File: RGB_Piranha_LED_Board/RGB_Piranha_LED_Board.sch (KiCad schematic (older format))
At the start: 20 parts, among them J1 Conn_01x04, J2 Conn_01x04

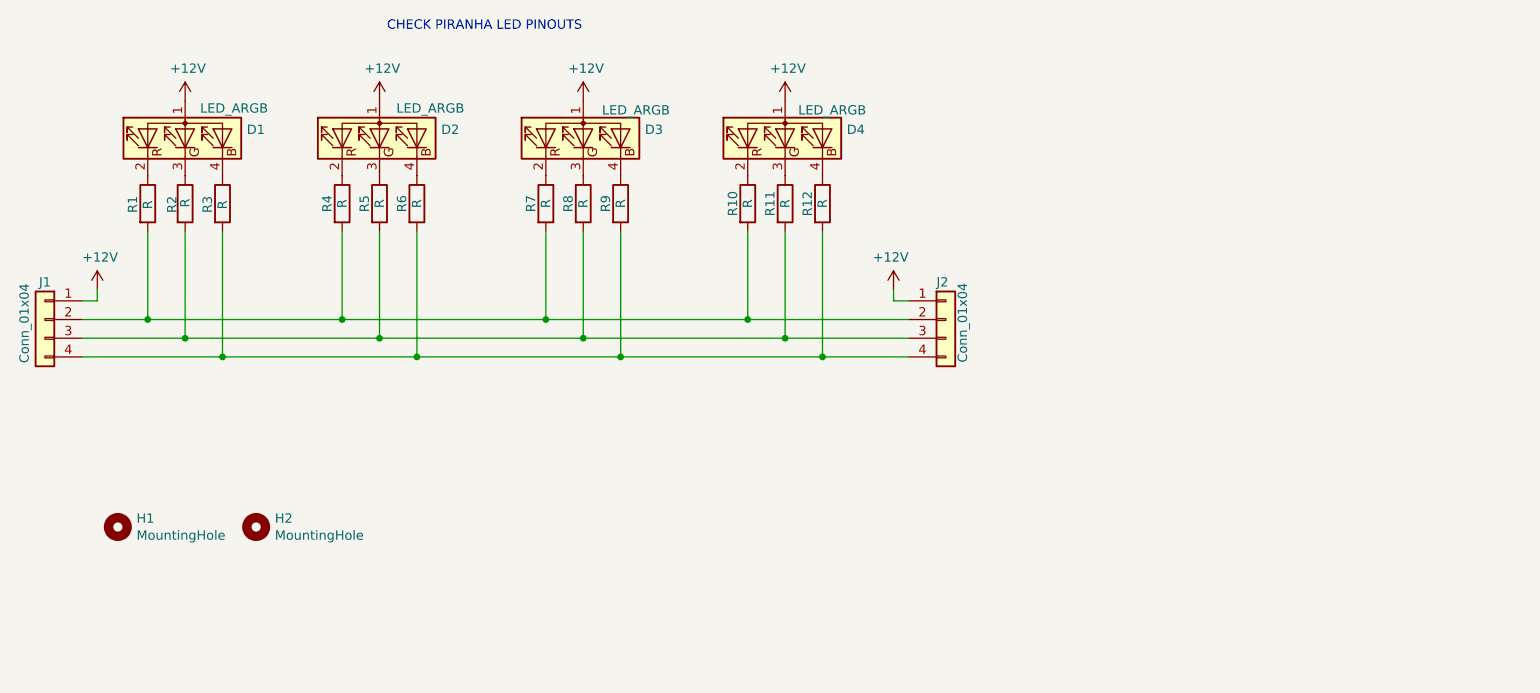
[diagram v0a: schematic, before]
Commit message: added custom LED footprint
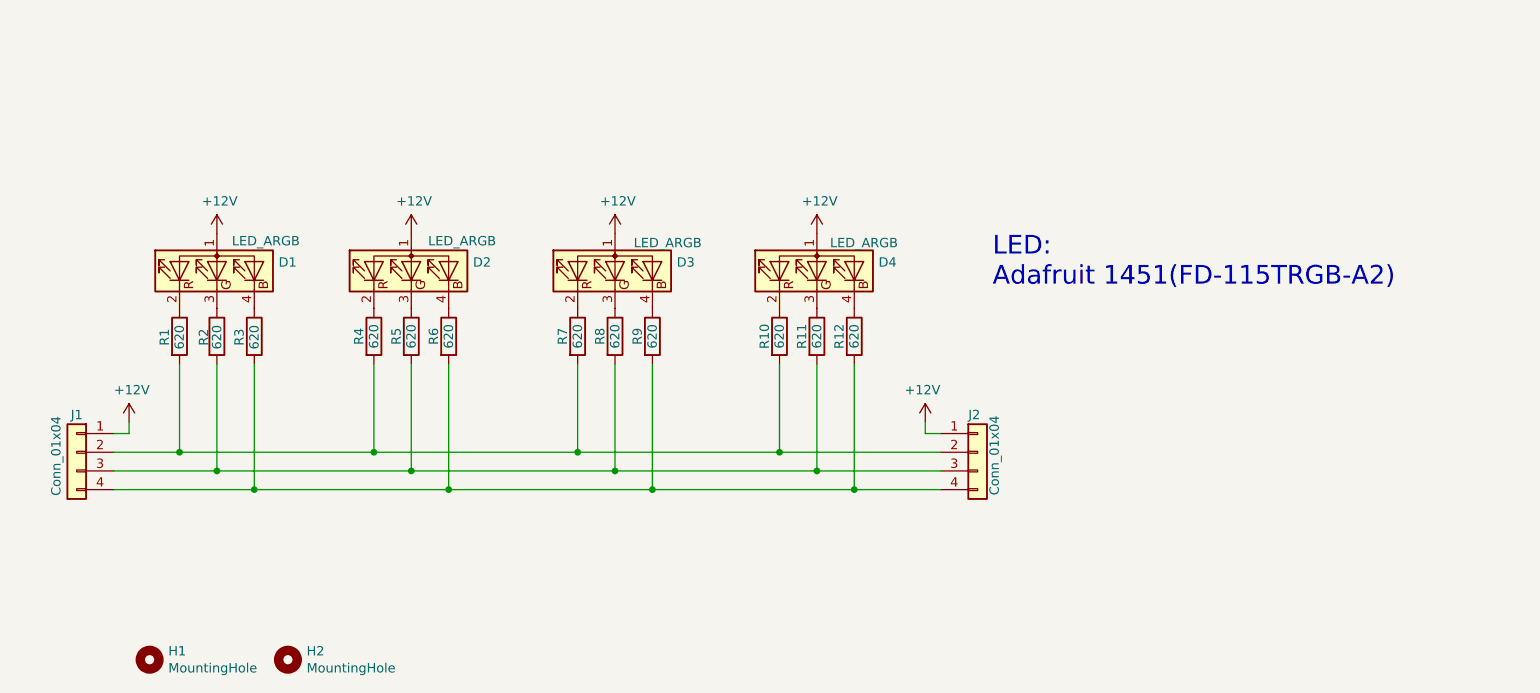
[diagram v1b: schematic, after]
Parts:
- D1, D2, D3, D4: footprint LED_THT:LED_BL-FL7680RGB -> RGB LED Piranha Super-Flux:LED_FD-115TRGB-A2
- R1, R10, R11, R12, R2, R3, R4, R5, R6, R7, R8, R9: value R -> 620; footprint Resistor_THT:R_Axial_DIN0207_L6.3mm_D2.5mm_P7.62mm_Horizontal -> Resistor_THT:R_Axial_DIN0309_L9.0mm_D3.2mm_P12.70mm_Horizontal
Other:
- note added: "LED:\nAdafruit 1451(FD-115TRGB-A2)"
- note removed: "CHECK PIRANHA LED PINOUTS"
- moved on the sheet: D1, D2, D3, D4, H1, H2, J1, J2, R1, R10, R11, R12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

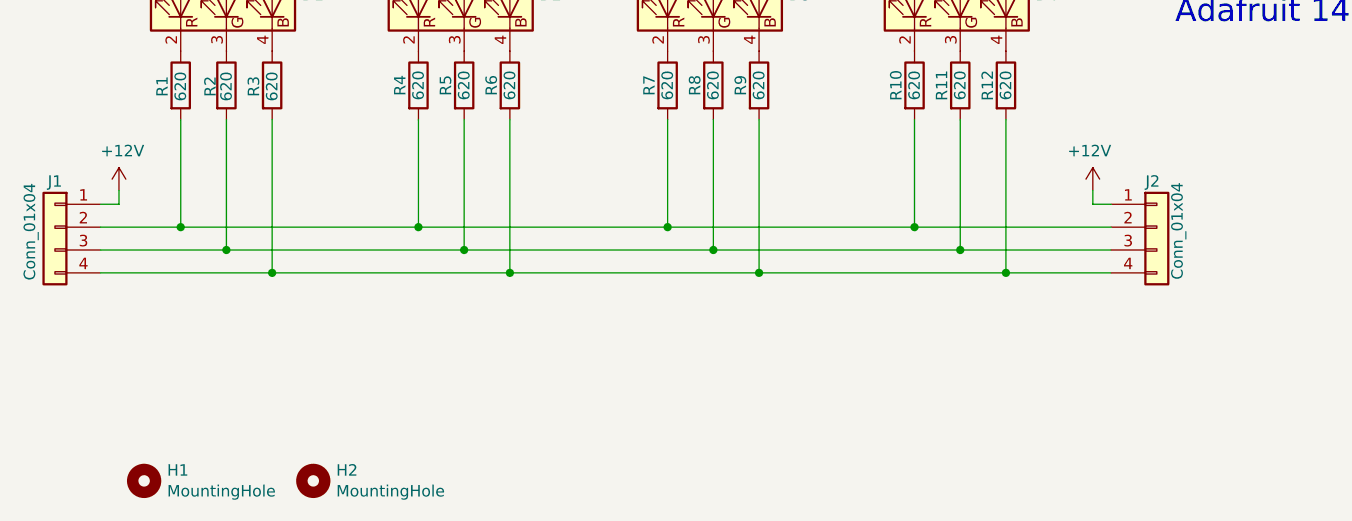
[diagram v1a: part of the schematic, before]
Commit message: changed THT resistors to SMD
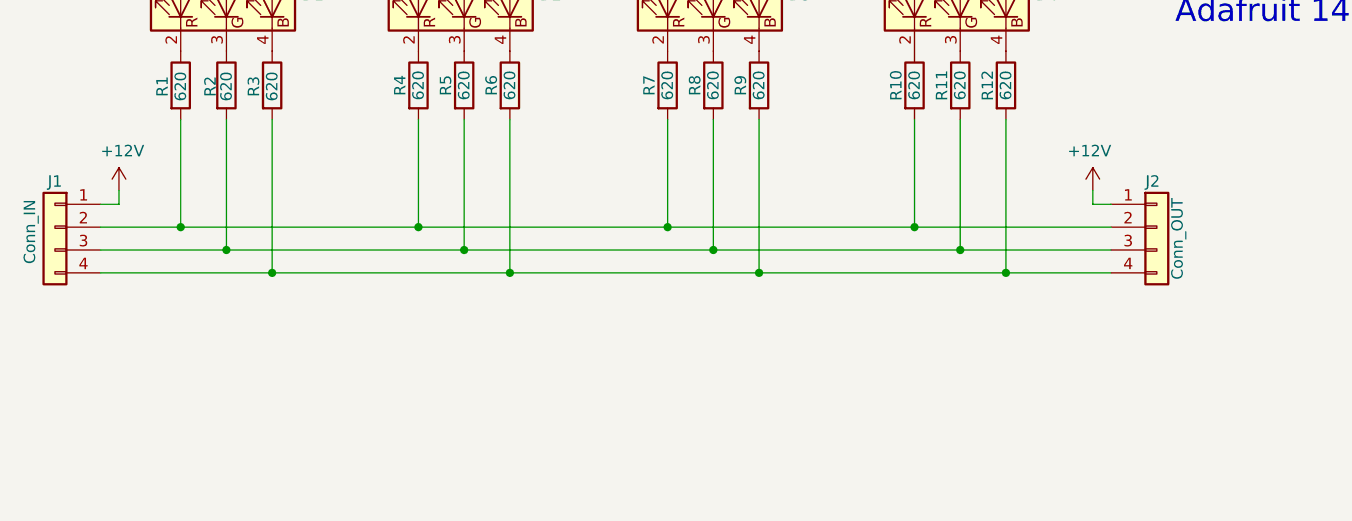
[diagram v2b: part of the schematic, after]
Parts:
- removed H1, H2: MountingHole, MountingHole:MountingHole_2.5mm, symbol Mechanical:MountingHole
- J1: value Conn_01x04 -> Conn_IN
- J2: value Conn_01x04 -> Conn_OUT
- R1, R10, R11, R12, R2, R3, R4, R5, R6, R7, R8, R9: footprint Resistor_THT:R_Axial_DIN0309_L9.0mm_D3.2mm_P12.70mm_Horizontal -> Resistor_SMD:R_1210_3225Metric_Pad1.42x2.65mm_HandSolder
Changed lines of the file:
@@
 EESchema Schematic File Version 4
+LIBS:RGB_Piranha_LED_Board-cache
 EELAYER 29 0
 EELAYER END
@@
 F 0 "R1" V 3720 3570 50  0000 L CNN
 F 1 "620" V 3800 3550 50  0000 L CNN
-F 2 "Resistor_THT:R_Axial_DIN0309_L9.0mm_D3.2mm_P12.70mm_Horizontal" V 3730 3620 50  0001 C CNN
+F 2 "Resistor_SMD:R_1210_3225Metric_Pad1.42x2.65mm_HandSolder" V 3730 3620 50  0001 C CNN
 F 3 "~" H 3800 3620 50  0001 C CNN
 	1    3800 3620
@@
 F 0 "R2" V 3930 3570 50  0000 L CNN
 F 1 "620" V 4000 3550 50  0000 L CNN
-F 2 "Resistor_THT:R_Axial_DIN0309_L9.0mm_D3.2mm_P12.70mm_Horizontal" V 3930 3620 50  0001 C CNN
+F 2 "Resistor_SMD:R_1210_3225Metric_Pad1.42x2.65mm_HandSolder" V 3930 3620 50  0001 C CNN
 F 3 "~" H 4000 3620 50  0001 C CNN
 	1    4000 3620
@@
 F 0 "R3" V 4120 3570 50  0000 L CNN
 F 1 "620" V 4200 3550 50  0000 L CNN
-F 2 "Resistor_THT:R_Axial_DIN0309_L9.0mm_D3.2mm_P12.70mm_Horizontal" V 4130 3620 50  0001 C CNN
+F 2 "Resistor_SMD:R_1210_3225Metric_Pad1.42x2.65mm_HandSolder" V 4130 3620 50  0001 C CNN
 F 3 "~" H 4200 3620 50  0001 C CNN
 	1    4200 3620
@@
 P 3250 4240
 F 0 "J1" H 3250 4440 50  0000 C CNN
-F 1 "Conn_01x04" V 3360 4220 50  0000 C CNN
+F 1 "Conn_IN" V 3360 4220 50  0000 C CNN
 F 2 "Connector_PinHeader_2.54mm:PinHeader_1x04_P2.54mm_Vertical" H 3250 4240 50  0001 C CNN
 F 3 "~" H 3250 4240 50  0001 C CNN
@@
 P 8070 4240
 F 0 "J2" H 8020 4440 50  0000 L CNN
-F 1 "Conn_01x04" V 8160 4010 50  0000 L CNN
+F 1 "Conn_OUT" V 8160 4010 50  0000 L CNN
 F 2 "Connector_PinSocket_2.54mm:PinSocket_1x04_P2.54mm_Vertical" H 8070 4240 50  0001 C CNN
 F 3 "~" H 8070 4240 50  0001 C CNN
@@
 F 0 "R4" V 4760 3620 50  0000 C CNN
 F 1 "620" V 4840 3620 50  0000 C CNN
-F 2 "Resistor_THT:R_Axial_DIN0309_L9.0mm_D3.2mm_P12.70mm_Horizontal" V 4770 3620 50  0001 C CNN
+F 2 "Resistor_SMD:R_1210_3225Metric_Pad1.42x2.65mm_HandSolder" V 4770 3620 50  0001 C CNN
 F 3 "~" H 4840 3620 50  0001 C CNN
 	1    4840 3620
@@
 F 0 "R5" V 4960 3620 50  0000 C CNN
 F 1 "620" V 5040 3620 50  0000 C CNN
-F 2 "Resistor_THT:R_Axial_DIN0309_L9.0mm_D3.2mm_P12.70mm_Horizontal" V 4970 3620 50  0001 C CNN
+F 2 "Resistor_SMD:R_1210_3225Metric_Pad1.42x2.65mm_HandSolder" V 4970 3620 50  0001 C CNN
 F 3 "~" H 5040 3620 50  0001 C CNN
 	1    5040 3620
@@
 F 0 "R6" V 5160 3620 50  0000 C CNN
 F 1 "620" V 5240 3620 50  0000 C CNN
-F 2 "Resistor_THT:R_Axial_DIN0309_L9.0mm_D3.2mm_P12.70mm_Horizontal" V 5170 3620 50  0001 C CNN
+F 2 "Resistor_SMD:R_1210_3225Metric_Pad1.42x2.65mm_HandSolder" V 5170 3620 50  0001 C CNN
 F 3 "~" H 5240 3620 50  0001 C CNN
 	1    5240 3620
@@
 F 0 "R7" V 5850 3620 50  0000 C CNN
 F 1 "620" V 5930 3620 50  0000 C CNN
-F 2 "Resistor_THT:R_Axial_DIN0309_L9.0mm_D3.2mm_P12.70mm_Horizontal" V 5860 3620 50  0001 C CNN
+F 2 "Resistor_SMD:R_1210_3225Metric_Pad1.42x2.65mm_HandSolder" V 5860 3620 50  0001 C CNN
 F 3 "~" H 5930 3620 50  0001 C CNN
 	1    5930 3620
@@
 F 0 "R8" V 6050 3620 50  0000 C CNN
 F 1 "620" V 6130 3620 50  0000 C CNN
-F 2 "Resistor_THT:R_Axial_DIN0309_L9.0mm_D3.2mm_P12.70mm_Horizontal" V 6060 3620 50  0001 C CNN
+F 2 "Resistor_SMD:R_1210_3225Metric_Pad1.42x2.65mm_HandSolder" V 6060 3620 50  0001 C CNN
 F 3 "~" H 6130 3620 50  0001 C CNN
 	1    6130 3620
@@
 F 0 "R9" V 6250 3620 50  0000 C CNN
 F 1 "620" V 6330 3620 50  0000 C CNN
-F 2 "Resistor_THT:R_Axial_DIN0309_L9.0mm_D3.2mm_P12.70mm_Horizontal" V 6260 3620 50  0001 C CNN
+F 2 "Resistor_SMD:R_1210_3225Metric_Pad1.42x2.65mm_HandSolder" V 6260 3620 50  0001 C CNN
 F 3 "~" H 6330 3620 50  0001 C CNN
 	1    6330 3620
@@
 F 0 "R10" V 6930 3620 50  0000 C CNN
 F 1 "620" V 7010 3620 50  0000 C CNN
-F 2 "Resistor_THT:R_Axial_DIN0309_L9.0mm_D3.2mm_P12.70mm_Horizontal" V 6940 3620 50  0001 C CNN
+F 2 "Resistor_SMD:R_1210_3225Metric_Pad1.42x2.65mm_HandSolder" V 6940 3620 50  0001 C CNN
 F 3 "~" H 7010 3620 50  0001 C CNN
 	1    7010 3620
@@
 F 0 "R11" V 7130 3620 50  0000 C CNN
 F 1 "620" V 7210 3620 50  0000 C CNN
-F 2 "Resistor_THT:R_Axial_DIN0309_L9.0mm_D3.2mm_P12.70mm_Horizontal" V 7140 3620 50  0001 C CNN
+F 2 "Resistor_SMD:R_1210_3225Metric_Pad1.42x2.65mm_HandSolder" V 7140 3620 50  0001 C CNN
 F 3 "~" H 7210 3620 50  0001 C CNN
 	1    7210 3620
@@
 F 0 "R12" V 7330 3620 50  0000 C CNN
 F 1 "620" V 7410 3620 50  0000 C CNN
-F 2 "Resistor_THT:R_Axial_DIN0309_L9.0mm_D3.2mm_P12.70mm_Horizontal" V 7340 3620 50  0001 C CNN
+F 2 "Resistor_SMD:R_1210_3225Metric_Pad1.42x2.65mm_HandSolder" V 7340 3620 50  0001 C CNN
 F 3 "~" H 7410 3620 50  0001 C CNN
 	1    7410 3620
@@
 	1    0    0    -1
 $EndComp
-$Comp
-L Mechanical:MountingHole H1
-U 1 1 634BDEFD
-P 3640 5350
-F 0 "H1" H 3740 5396 50  0000 L CNN
-F 1 "MountingHole" H 3740 5305 50  0000 L CNN
-F 2 "MountingHole:MountingHole_2.5mm" H 3640 5350 50  0001 C CNN
-F 3 "~" H 3640 5350 50  0001 C CNN
-	1    3640 5350
-	1    0    0    -1
-$EndComp
-$Comp
-L Mechanical:MountingHole H2
-U 1 1 634BEC96
-P 4380 5350
-F 0 "H2" H 4480 5396 50  0000 L CNN
-F 1 "MountingHole" H 4480 5305 50  0000 L CNN
-F 2 "MountingHole:MountingHole_2.5mm" H 4380 5350 50  0001 C CNN
-F 3 "~" H 4380 5350 50  0001 C CNN
-	1    4380 5350
-	1    0    0    -1
-$EndComp
